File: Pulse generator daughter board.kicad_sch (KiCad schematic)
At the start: 71 parts, among them J1 Vin1, J10 Vin2_GND, J11 CN8, J12 CN9, J13 CN7, J14 CN10, J15 CH1 output, J16 GND, J17 CH2 output, J18 GND, J2 Vin1_GND, J3 3V3, J4 DVM1, J5 3V3, J6 DVM1, J7 T+, J8 T-, J9 Vin2, U1 RYK-053.3SH, U2 MAX31855KASA, U3 ADUM1402, U4 TC4427, U5 TC4427

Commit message: Positioning done
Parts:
- removed C3: 10nF, Capacitor_SMD:C_0805_2012Metric_Pad1.18x1.45mm_HandSolder, symbol Device:C
- removed J3, J5: 3V3, Connector_Wire:SolderWire-0.5sqmm_1x01_D0.9mm_OD2.1mm, symbol Connector:Conn_01x01_Socket
- removed U2: MAX31855KASA, Package_SO:SOIC-8_3.9x4.9mm_P1.27mm, symbol Sensor_Temperature:MAX31855KASA
- removed U3: ADUM1402, Package_SO:SOIC-16W_7.5x10.3mm_P1.27mm, symbol Rafal_Library:ADUM1402
- added C18, C19, C4: 100nF, Capacitor_SMD:C_0805_2012Metric_Pad1.18x1.45mm_HandSolder, symbol Rafal_Library:C
- added C5, C7: 10nF, Capacitor_SMD:C_0805_2012Metric_Pad1.18x1.45mm_HandSolder, symbol Rafal_Library:C
- added D10, D9: 20V, Diode_SMD:D_SOD-323F, symbol Rafal_Library:D_Zener
- added J10, J21, J22, J8: GND, Connector_Wire:SolderWire-0.5sqmm_1x01_D0.9mm_OD2.1mm, symbol Rafal_Library:Conn_01x01_Socket
- added J11: Power_on LED, Connector_Wire:SolderWire-0.5sqmm_1x01_D0.9mm_OD2.1mm, symbol Rafal_Library:Conn_01x01_Socket
- added J12: Power_on LED_ret, Connector_Wire:SolderWire-0.5sqmm_1x01_D0.9mm_OD2.1mm, symbol Rafal_Library:Conn_01x01_Socket
- added J23, J24: Switch_1, Connector_Wire:SolderWire-0.5sqmm_1x01_D0.9mm_OD2.1mm, symbol Rafal_Library:Conn_01x01_Socket
- added R1, R2: R, Resistor_SMD:R_0805_2012Metric_Pad1.20x1.40mm_HandSolder, symbol Rafal_Library:R
- added R19, R20, R23, R24: DNF, Resistor_SMD:R_0805_2012Metric_Pad1.20x1.40mm_HandSolder, symbol Rafal_Library:R
- added R33, R34, R35, R36: 43R, Resistor_SMD:R_2512_6332Metric_Pad1.40x3.35mm_HandSolder, symbol Rafal_Library:R
- added R5: 10k, Resistor_SMD:R_0805_2012Metric_Pad1.20x1.40mm_HandSolder, symbol Rafal_Library:R
- added TR1, TR2: RQ5H020TNTL, Rafal:SOT-346T, symbol Rafal_Library:RQ5H020TNTL
- added U2: MAX31856, Package_SO:TSSOP-14_4.4x5mm_P0.65mm, symbol Rafal_Library:MAX31856
- added U3: ADuM1401xRW, Package_SO:SOIC-16W_7.5x10.3mm_P1.27mm, symbol Rafal_Library:ADuM1401xRW
- C1, C2: symbol Device:C -> Rafal_Library:C
- C10: renamed from C7; symbol Device:C -> Rafal_Library:C
- C11: renamed from C8; symbol Device:C -> Rafal_Library:C
- C12: renamed from C10; symbol Device:C -> Rafal_Library:C
- C13: renamed from C11; symbol Device:C -> Rafal_Library:C
- C14: renamed from C12; symbol Device:C -> Rafal_Library:C
- C15: renamed from C13; symbol Device:C -> Rafal_Library:C
- C16: renamed from C14; symbol Device:C -> Rafal_Library:C
- C17: renamed from C15; symbol Device:C -> Rafal_Library:C
- C3: renamed from C9; symbol Device:C -> Rafal_Library:C
- C6: renamed from C4; symbol Device:C -> Rafal_Library:C
- C8: renamed from C6; symbol Device:C -> Rafal_Library:C
- C9: renamed from C5; symbol Device:C -> Rafal_Library:C
- D1, D7, D8: symbol Device:D_Zener -> Rafal_Library:D_Zener
- D2: renamed from D6; symbol Device:D_Zener -> Rafal_Library:D_Zener
- D3: renamed from D2; symbol Device:D_Zener -> Rafal_Library:D_Zener
- D4: renamed from D9; symbol Device:D_Zener -> Rafal_Library:D_Zener
- D5: renamed from D3; symbol Device:D_Zener -> Rafal_Library:D_Zener
- D6: renamed from D4; symbol Device:D_Zener -> Rafal_Library:D_Zener
- J1: renamed from J7; symbol Connector:Conn_01x01_Socket -> Rafal_Library:Conn_01x01_Socket
- J13: renamed from J11; symbol Connector_Generic:Conn_02x08_Odd_Even -> Rafal_Library:Conn_02x08_Odd_Even
- J14: renamed from J12; symbol Connector_Generic:Conn_02x15_Odd_Even -> Rafal_Library:Conn_02x15_Odd_Even
- J15: renamed from J13; symbol Connector_Generic:Conn_02x10_Odd_Even -> Rafal_Library:Conn_02x10_Odd_Even
- J16: renamed from J14; symbol Connector_Generic:Conn_02x17_Odd_Even -> Rafal_Library:Conn_02x17_Odd_Even
- J17: renamed from J15; symbol Connector:Conn_01x01_Socket -> Rafal_Library:Conn_01x01_Socket
- J18: renamed from J16; symbol Connector:Conn_01x01_Socket -> Rafal_Library:Conn_01x01_Socket
- J19: renamed from J17; symbol Connector:Conn_01x01_Socket -> Rafal_Library:Conn_01x01_Socket
- J2: renamed from J8; symbol Connector:Conn_01x01_Socket -> Rafal_Library:Conn_01x01_Socket
- J20: renamed from J18; symbol Connector:Conn_01x01_Socket -> Rafal_Library:Conn_01x01_Socket
- J3: renamed from J1; value Vin1 -> Vin1_PSU; symbol Connector:Conn_01x01_Socket -> Rafal_Library:Conn_01x01_Socket
- J4: renamed from J2; symbol Connector:Conn_01x01_Socket -> Rafal_Library:Conn_01x01_Socket
- J5: renamed from J9; value Vin2 -> Vin2_PSU; symbol Connector:Conn_01x01_Socket -> Rafal_Library:Conn_01x01_Socket
- J6: renamed from J10; symbol Connector:Conn_01x01_Socket -> Rafal_Library:Conn_01x01_Socket
- J7: renamed from J4; symbol Connector:Conn_01x01_Socket -> Rafal_Library:Conn_01x01_Socket
- J9: renamed from J6; symbol Connector:Conn_01x01_Socket -> Rafal_Library:Conn_01x01_Socket
- R10: renamed from R3; symbol Device:R -> Rafal_Library:R
- R11: renamed from R8; symbol Device:R -> Rafal_Library:R
- R12: renamed from R9; symbol Device:R -> Rafal_Library:R
- R13: renamed from R10; symbol Device:R -> Rafal_Library:R
- R14: renamed from R11; symbol Device:R -> Rafal_Library:R
- R15: renamed from R12; symbol Device:R -> Rafal_Library:R
- R16: renamed from R13; symbol Device:R -> Rafal_Library:R
- R17: renamed from R14; symbol Device:R -> Rafal_Library:R
- R18: renamed from R15; symbol Device:R -> Rafal_Library:R
- R21: renamed from R16; symbol Device:R -> Rafal_Library:R
- R22: renamed from R17; symbol Device:R -> Rafal_Library:R
- R25: renamed from R18; symbol Device:R -> Rafal_Library:R
- R26: renamed from R19; symbol Device:R -> Rafal_Library:R
- R27: renamed from R20; symbol Device:R -> Rafal_Library:R
- R28: renamed from R21; symbol Device:R -> Rafal_Library:R
- R29: renamed from R22; symbol Device:R -> Rafal_Library:R
- R3: renamed from R1; symbol Device:R -> Rafal_Library:R
- R30: renamed from R23; symbol Device:R -> Rafal_Library:R
- R31: renamed from R24; symbol Device:R -> Rafal_Library:R
- R32: renamed from R25; symbol Device:R -> Rafal_Library:R
- R4: renamed from R2; symbol Device:R -> Rafal_Library:R
- R6: renamed from R4; symbol Device:R -> Rafal_Library:R
- R7: renamed from R5; symbol Device:R -> Rafal_Library:R
- R8: renamed from R6; symbol Device:R -> Rafal_Library:R
- R9: renamed from R7; symbol Device:R -> Rafal_Library:R
- U4, U5: symbol Driver_FET:MIC4427 -> Rafal_Library:MIC4427
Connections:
- net +3V3: now also C10.1, C11.1, J13.7 (Pin_7), R11.1, R13.1, U3.1 (VDD1), U3.7 (VE1)
- net GND: now also J13.11 (Pin_11), J13.13 (Pin_13), J14.12 (Pin_12), J14.23 (Pin_23), J15.8 (Pin_8), J16.17 (Pin_17), J16.22 (Pin_22), J16.27 (Pin_27), J16.5 (Pin_5), C18.2, C19.2, D10.2 (A), D9.2 (A), J10.1 (Pin_1), J12.1 (Pin_1), J21.1 (Pin_1), J22.1 (Pin_1), J8.1 (Pin_1), R23.2, R24.2, TR1.2, TR2.2, U3.2 (GND1), U3.8 (GND1)
- net OV_TC: now also C5.2, C7.2, U2.1 (AGND), U2.14 (DGND), U3.15 (GND2), U3.9 (GND2)
- net Vin1: now also J13.15 (Pin_15), R5.1
- net SPI_MOSI: now reaches J15.14 (Pin_14)
- net SPI_MOSI: now also U3.3 (VIA)
- net SPI1_SCLK: now reaches J15.15 (Pin_15)
- net SPI1_SCLK: now also U3.4 (VIB)
- net SPI1_MISO: now reaches J15.19 (Pin_19)
- net SPI1_MISO: now also U3.6 (VOD)
- net SPI1_CS: now reaches J15.2 (Pin_2)
- net SPI1_CS: now also U3.5 (VIC)
- net at C14.1, C6.1, C8.1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: now also U2.5 (AVDD), U2.8 (DVDD), U3.10 (VE2), U3.16 (VDD2)
- net at J1.1 (Pin_1): now also R1.1
- net at J2.1 (Pin_1): now also R2.1, U2.2 (BIAS)
- net Switch_1: now reaches J16.14 (Pin_14)
- net Switch_1: now also R19.2
- net Switch_2: now reaches J16.16 (Pin_16)
- net Switch_2: now also R20.2
- new net: C19.1, R20.1, R24.1, TR2.1
- new net: C4.1, C7.1, R1.2, U2.4 (T+)
- new net: J11.1 (Pin_1), R5.2
- new net: D9.1 (K), J24.1 (Pin_1), R33.2, R34.2
- new net: R35.1, R36.1, TR2.3
- new net: D10.1 (K), J23.1 (Pin_1), R35.2, R36.2
- new net: U2.11 (SDO), U3.11 (VID)
- new net: U2.9 (~{CS}), U3.12 (VOC)
- new net: U2.10 (SCK), U3.13 (VOB)
- new net: U2.12 (SDI), U3.14 (VOA)
- new net: C4.2, C5.1, R2.2, U2.3 (T-)
- new net: R33.1, R34.1, TR1.3
- new net: C18.1, R19.1, R23.1, TR1.1
- no-connect marks 0 -> 82
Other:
- note added: "Add resistors, capacitor on layout for EMI Add switches refill planes"
- note added: "Vin1 supplies STM32"
- moved on the sheet: C1, C14, C15, C3, C6, C8, C9, D2, J1, J15, J16, J2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

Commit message: LAyout finished
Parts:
- added C20: EMI cap, Capacitor_SMD:C_0805_2012Metric_Pad1.18x1.45mm_HandSolder, symbol Rafal_Library:C
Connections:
- net GND: now also C20.1
- net OV_TC: now also C20.2
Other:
- note removed: "Add resistors, capacitor on layout for EMI Add switches refill planes"
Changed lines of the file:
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@@
 	)
 	(junction
+		(at 48.26 186.69)
+		(diameter 0)
+		(color 0 0 0 0)
+	)
+	(junction
 		(at 350.52 175.26)
 		(diameter 0)
@@
 	)
 	(junction
+		(at 30.48 186.69)
+		(diameter 0)
+		(color 0 0 0 0)
+	)
+	(junction
 		(at 52.07 186.69)
 		(diameter 0)
@@
 	(wire
 		(pts
+			(xy 30.48 196.85) (xy 30.48 186.69)
+		)
+		(stroke
+			(width 0)
+			(type default)
+		)
+	)
+	(wire
+		(pts
 			(xy 259.08 80.01) (xy 269.24 80.01)
 		)
@@
 	(wire
 		(pts
+			(xy 48.26 196.85) (xy 48.26 186.69)
+		)
+		(stroke
+			(width 0)
+			(type default)
+		)
+	)
+	(wire
+		(pts
 			(xy 199.39 151.13) (xy 236.22 151.13)
 		)
@@
 	(wire
 		(pts
+			(xy 35.56 196.85) (xy 30.48 196.85)
+		)
+		(stroke
+			(width 0)
+			(type default)
+		)
+	)
+	(wire
+		(pts
 			(xy 346.71 90.17) (xy 346.71 93.98)
 		)
@@
 	(wire
 		(pts
+			(xy 43.18 196.85) (xy 48.26 196.85)
+		)
+		(stroke
+			(width 0)
+			(type default)
+		)
+	)
+	(wire
+		(pts
 			(xy 323.85 80.01) (xy 328.93 80.01)
 		)
@@
 		)
 	)
-	(text "Add resistors, capacitor on layout for EMI\nAdd switches\nrefill planes"
-		(exclude_from_sim no)
-		(at 264.414 228.6 0)
-		(effects
-			(font
-				(size 1.27 1.27)
-			)
-		)
-	)
 	(text "Vin1 supplies STM32"
 		(exclude_from_sim no)
@@
 					(unit 1)
 				)
+			)
+		)
+	)
+	(symbol
+		(lib_id "Rafal_Library:C")
+		(at 39.37 196.85 90)
+		(unit 1)
+		(exclude_from_sim no)
+		(in_bom yes)
+		(on_board yes)
+		(dnp no)
+		(fields_autoplaced yes)
+		(property "Reference" "C20"
+			(at 39.37 189.23 90)
+			(effects
+				(font
+					(size 1.27 1.27)
+				)
+			)
+		)
+		(property "Value" "EMI cap"
+			(at 39.37 191.77 90)
+			(effects
+				(font
+					(size 1.27 1.27)
+				)
+			)
+		)
+		(property "Footprint" "Capacitor_SMD:C_0805_2012Metric_Pad1.18x1.45mm_HandSolder"
+			(at 43.18 195.8848 0)
+			(effects
+				(font
+					(size 1.27 1.27)
+				)
+				(hide yes)
+			)
+		)
+		(property "Datasheet" "~"
+			(at 39.37 196.85 0)
+			(effects
+				(font
+					(size 1.27 1.27)
+				)
+				(hide yes)
+			)
+		)
+		(property "Description" "Unpolarized capacitor"
+			(at 39.37 196.85 0)
+			(effects
+				(font
+					(size 1.27 1.27)
+				)
+				(hide yes)
+			)
+		)
+		(pin "1"
+		)
+		(pin "2"
+		)
+		(instances
+			(project "Pulse generator daughter board"
+				(path "/1303051a-0047-4158-8a91-4ef629dc783f"
+					(reference "C20")
+					(unit 1)
+				)

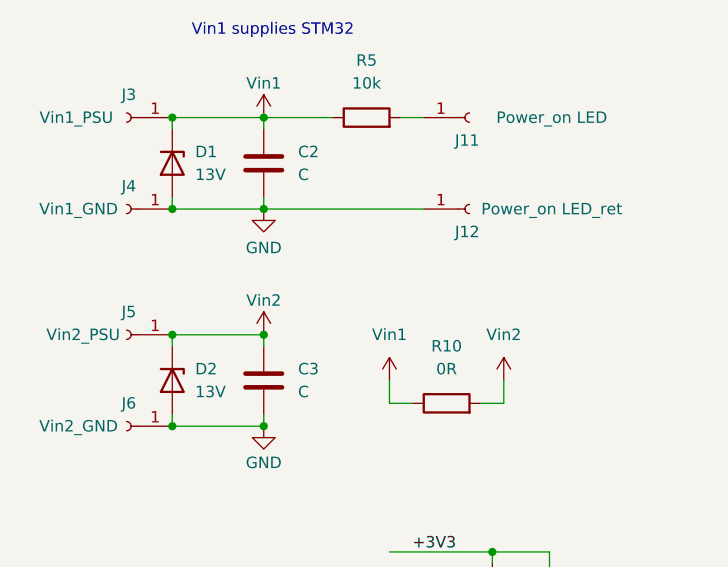
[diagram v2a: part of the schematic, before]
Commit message: 4 unconnected pads on PCB fixed
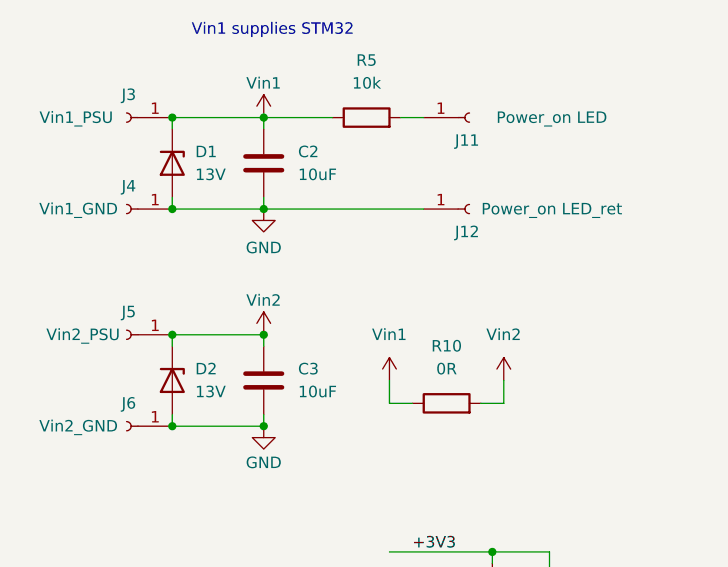
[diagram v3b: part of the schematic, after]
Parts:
- C2, C3: value C -> 10uF
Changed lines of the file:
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@@
 			)
 		)
-		(property "Value" "C"
+		(property "Value" "10uF"
 			(at 48.26 57.1499 0)
 			(effects
@@
 			)
 		)
-		(property "Value" "C"
+		(property "Value" "10uF"
 			(at 48.26 33.0199 0)
 			(effects
